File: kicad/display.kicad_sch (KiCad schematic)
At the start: 6 parts

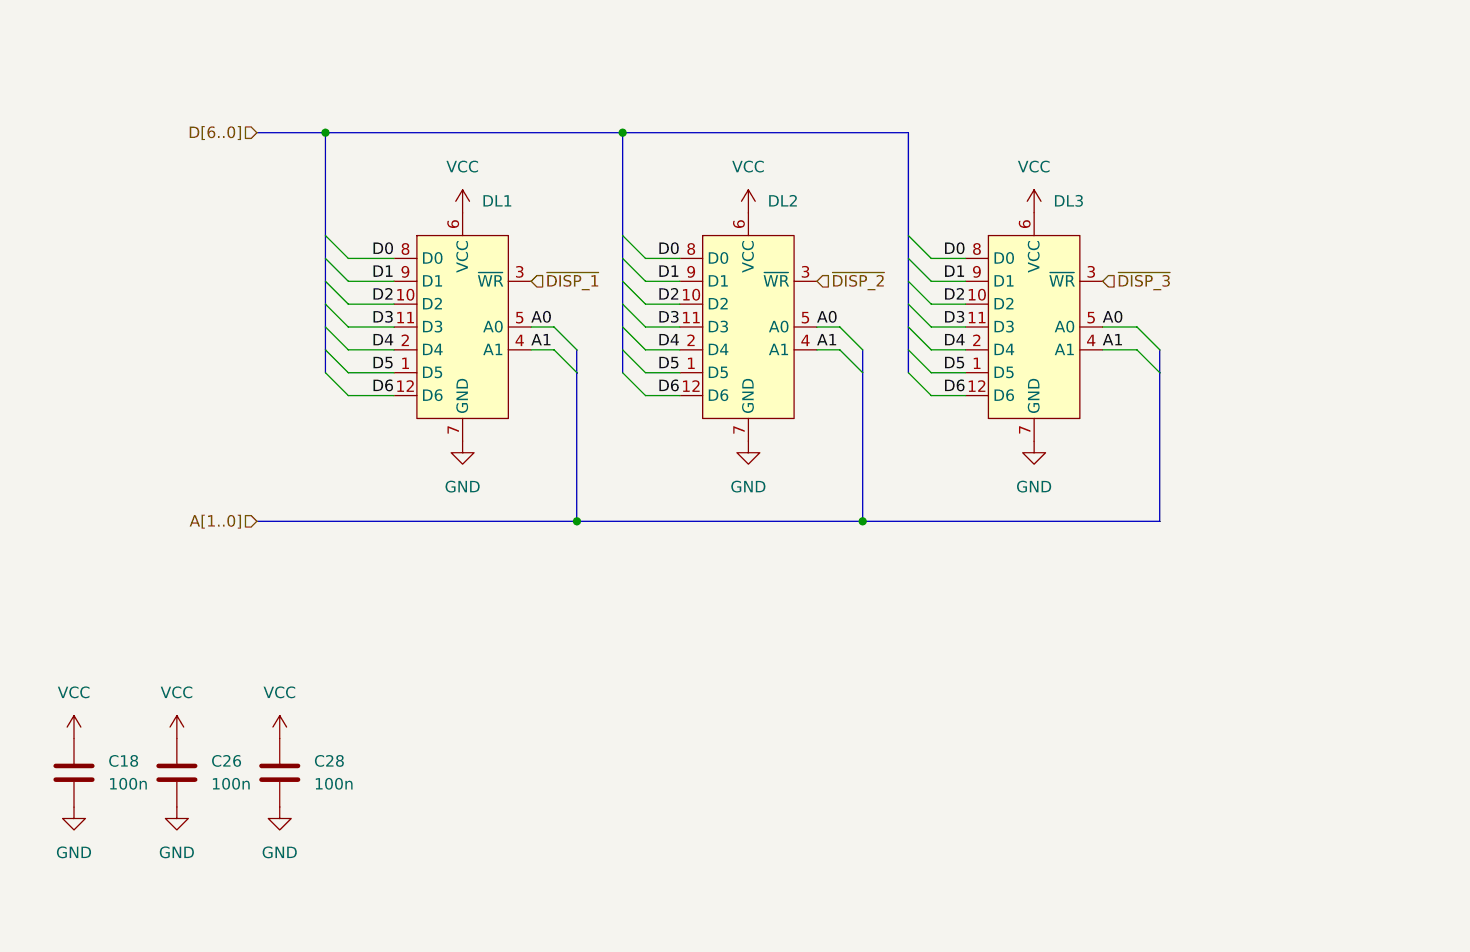
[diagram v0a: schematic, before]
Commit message: HW: Fix lack of /WR gating for DL1414
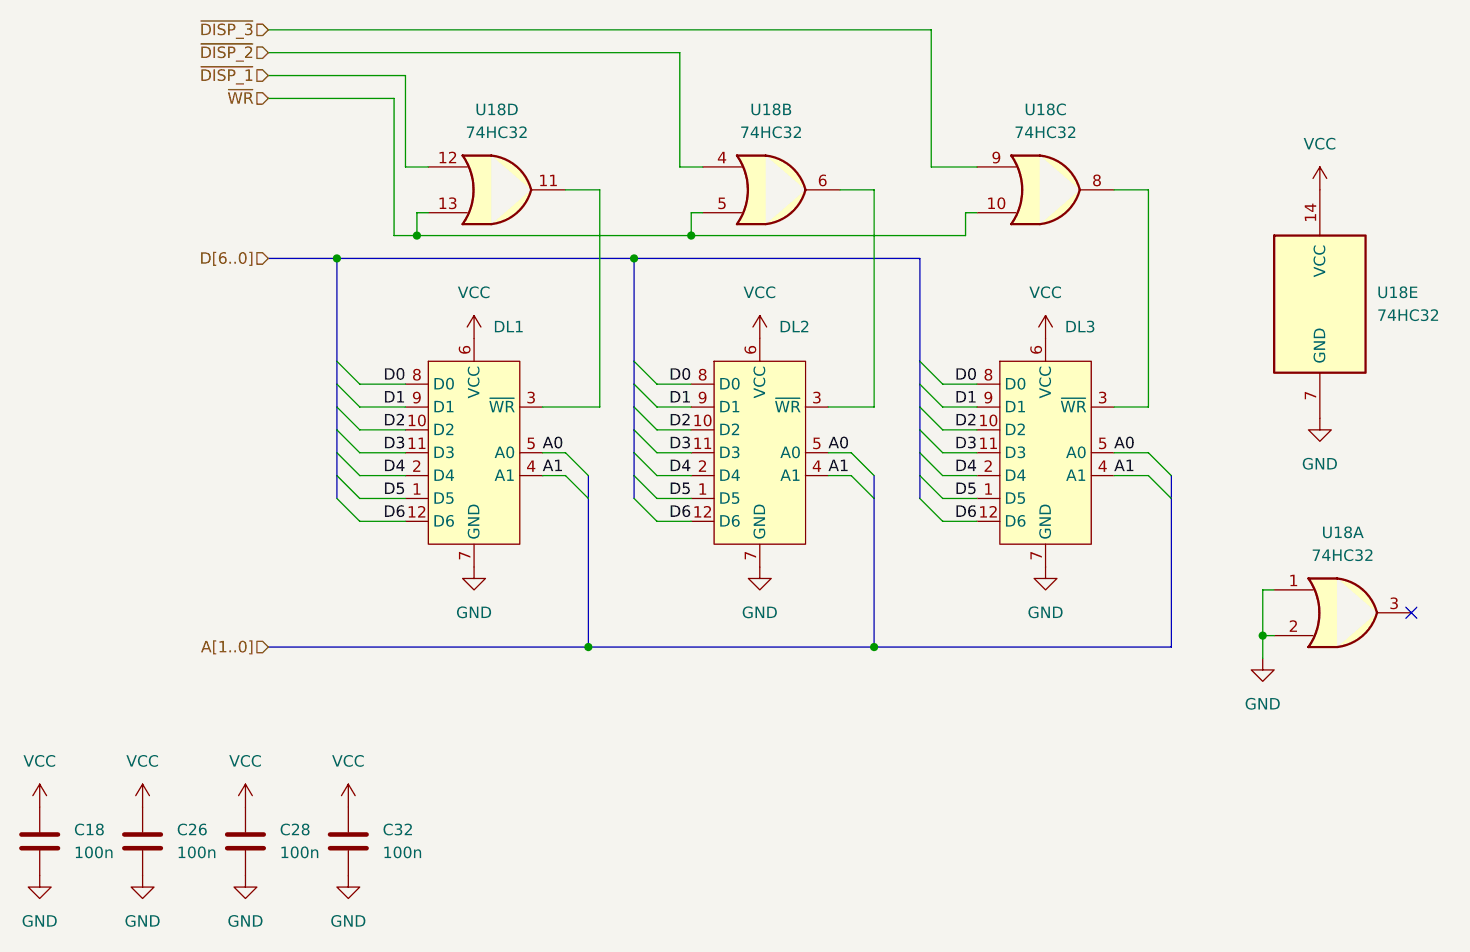
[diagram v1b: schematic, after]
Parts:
- added C32: 100n, Capacitor_SMD:C_0805_2012Metric, symbol Device:C
- added U18: 74HC32, Package_SO:SO-14_3.9x8.65mm_P1.27mm, symbol 74xx:74LS32
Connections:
- net GND: now also C32.2, U18.1, U18.2, U18.7 (GND)
- net VCC: now also C32.1, U18.14 (VCC)
- net ~{DISP_1}: now also U18.12; no longer DL1.3 (~{WR})
- net ~{DISP_2}: now also U18.4; no longer DL2.3 (~{WR})
- net ~{DISP_3}: now also U18.9; no longer DL3.3 (~{WR})
- new net: DL2.3 (~{WR}), U18.6
- new net: DL3.3 (~{WR}), U18.8
- new net: DL1.3 (~{WR}), U18.11
- new net ~{WR}: U18.10, U18.13, U18.5
- no-connect marks 0 -> 1
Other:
- moved on the sheet: C18, C26, C28, DL1, DL2, DL3
